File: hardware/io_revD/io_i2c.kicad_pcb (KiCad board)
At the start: 2 copper layers, 103.6 x 74.9 mm, 61 parts, among them J1 Target Interface, 2716 Pinout, J10 Conn_01x01, J11 Conn_01x01, J12 Conn_01x01, J13 Conn_01x01, J14 Conn_01x01, J15 Conn_01x01, J16 read region, J2 Jumper Block, J3 Jumper Block, J4 Target Interface, 2716 Pinout, J5 Conn_01x01, J6 Conn_01x01, J7 Conn_01x01, J8 Conn_01x01, J9 Conn_01x01, Q1 2N7000, U1 2716, U2 74HCT74, U3 74HCT125, U4 74HCT138, U6 MCP23018-E_SP, U7 74HCT138

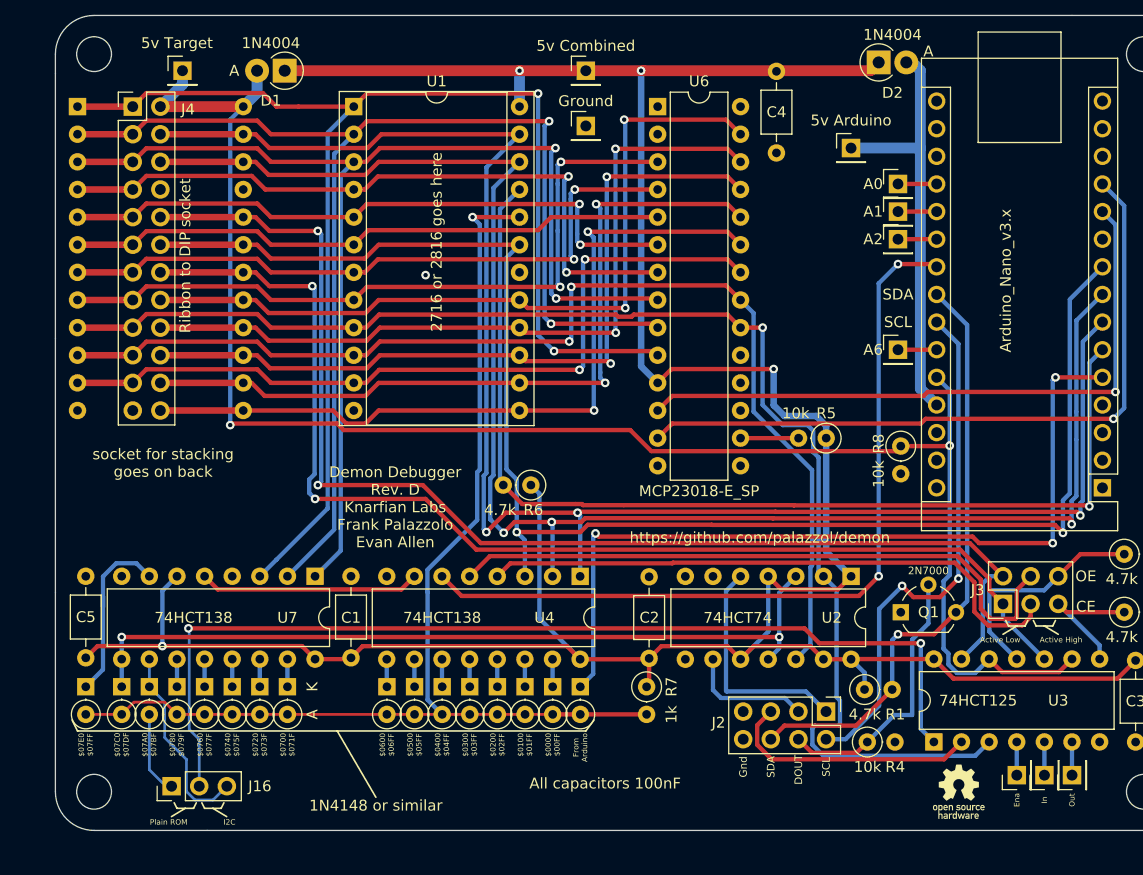
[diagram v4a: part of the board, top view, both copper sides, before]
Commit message: fixed silk, locations, and jumper
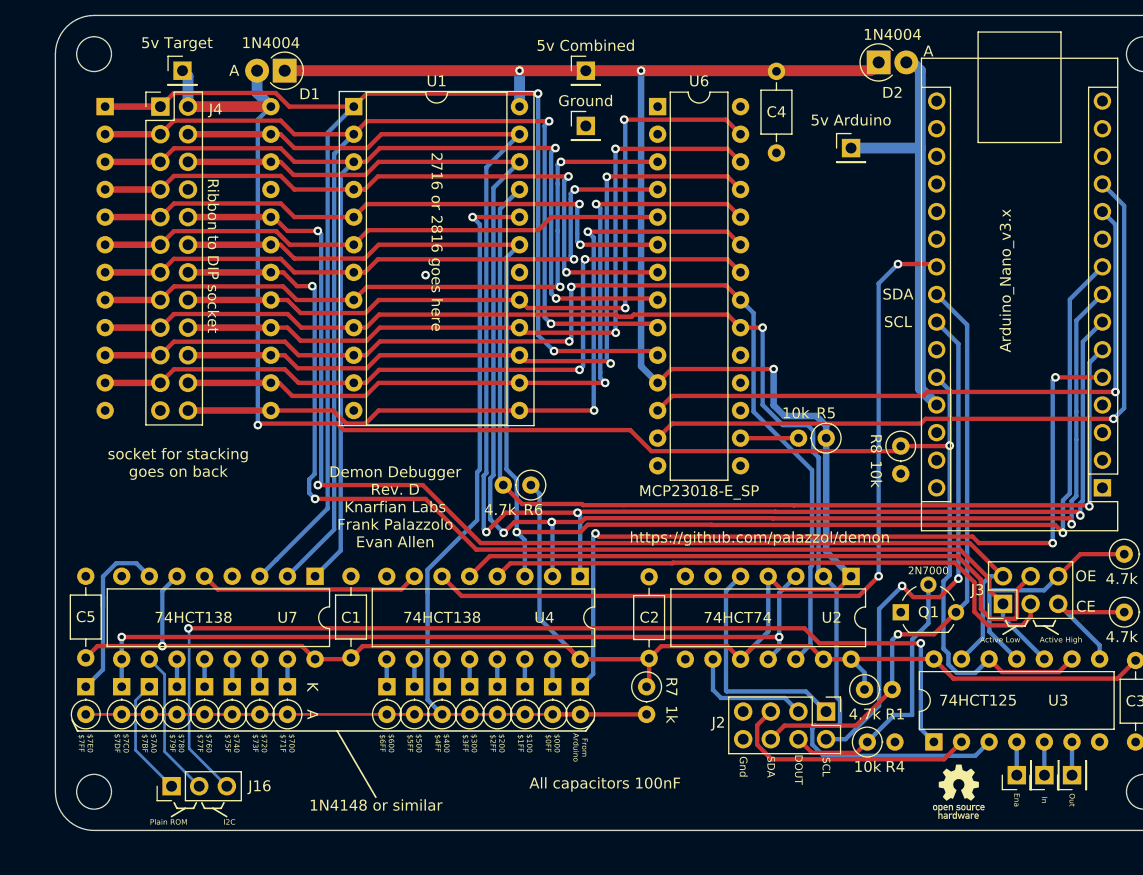
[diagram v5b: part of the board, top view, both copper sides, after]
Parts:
- removed J10, J11, J8, J9: Conn_01x01, Connector_PinHeader_2.54mm:PinHeader_1x01_P2.54mm_Vertical
- moved J1 2.54 mm to (89.2, 102.1)
- moved J4 2.54 mm to (94.2, 102.1)
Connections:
- A1 pad 19: Net-(A1-Pad19) -> unconnected-(A1-Pad19)
- A1 pad 20: Net-(A1-Pad20) -> unconnected-(A1-Pad20)
- A1 pad 21: Net-(A1-Pad21) -> unconnected-(A1-Pad21)
- A1 pad 25: Net-(A1-Pad25) -> unconnected-(A1-Pad25)
- D18 pad 1: Net-(U7-Pad10) -> Net-(D18-Pad1)
- D18 pad 2: Net-(D18-Pad2) -> Net-(D10-Pad2)
- J16 pad 1: Net-(D18-Pad2) -> Net-(D18-Pad1)
- J16 pad 2: Net-(U3-Pad1) -> Net-(U7-Pad10)
- J16 pad 3: Net-(U7-Pad10) -> Net-(J16-Pad3)
- U3 pad 1: Net-(U3-Pad1) -> Net-(J16-Pad3)
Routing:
- net Net-(J16-Pad3): track 0.00 -> 93.5 mm, vias 0 -> 2
- net Net-(U3-Pad1): track 92.4 -> 0.00 mm, vias 2 -> 0
- net Net-(D18-Pad1): track 0.00 -> 11.0 mm
- net Net-(D18-Pad2): track 7.76 -> 0.00 mm
- net Net-(U7-Pad10): track 18.1 -> 13.6 mm
- net Net-(A1-Pad25): track 3.56 -> 0.00 mm
- net Net-(A1-Pad21): track 3.56 -> 0.00 mm
- net Net-(A1-Pad20): track 3.56 -> 0.00 mm
- net Net-(A1-Pad19): track 3.56 -> 0.00 mm
- net +5VD: track 153.4 -> 150.2 mm
- net /Target OE: track 115.0 -> 112.4 mm
- net /D4: track 72.4 -> 69.9 mm
- net /A8: track 152.2 -> 149.7 mm
- net /A10: track 142.5 -> 140.0 mm
- net /Target CE: track 109.1 -> 106.5 mm
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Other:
- board text added: "$000 $0FF"
- board text added: "$100 $1FF"
- board text added: "$200 $2FF"
- board text added: "$300 $3FF"
- board text added: "$400 $4FF"
- board text added: "$500 $5FF"
- board text added: "$600 $6FF"
- board text added: "$700 $71F"
- board text added: "$720 $73F"
- board text added: "$740 $75F"
- board text added: "$760 $77F"
- board text added: "$780 $79F"
- board text added: "$7A0 $7BF"
- board text added: "$7C0 $7DF"
- board text added: "$7E0 $7FF"
- board text removed: "$0000 $00FF"
- board text removed: "$0100 $01FF"
- board text removed: "$0200 $02FF"
- board text removed: "$0300 $03FF"
- board text removed: "$0400 $04FF"
- board text removed: "$0500 $05FF"
- board text removed: "$0600 $06FF"
- board text removed: "$0700 $071F"
- board text removed: "$0720 $073F"
- board text removed: "$0740 $075F"
- board text removed: "$0760 $077F"
- board text removed: "$0780 $079F"
- board text removed: "$07A0 $07BF"
- board text removed: "$07C0 $07DF"
- board text removed: "$07E0 $07FF"
- board text removed: "A0"
- board text removed: "A1"
- board text removed: "A2"
- board text removed: "A6"

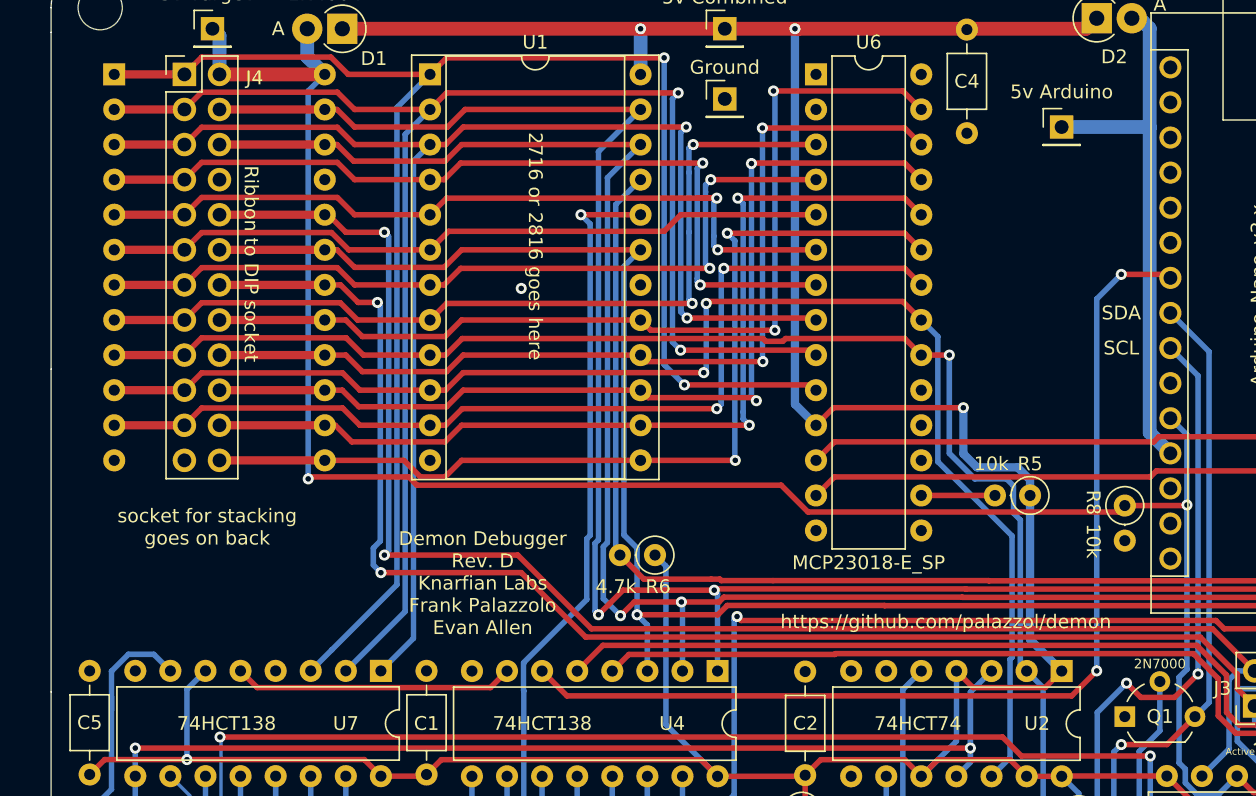
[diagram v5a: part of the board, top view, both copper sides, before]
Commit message: added layout change for extra CS mode
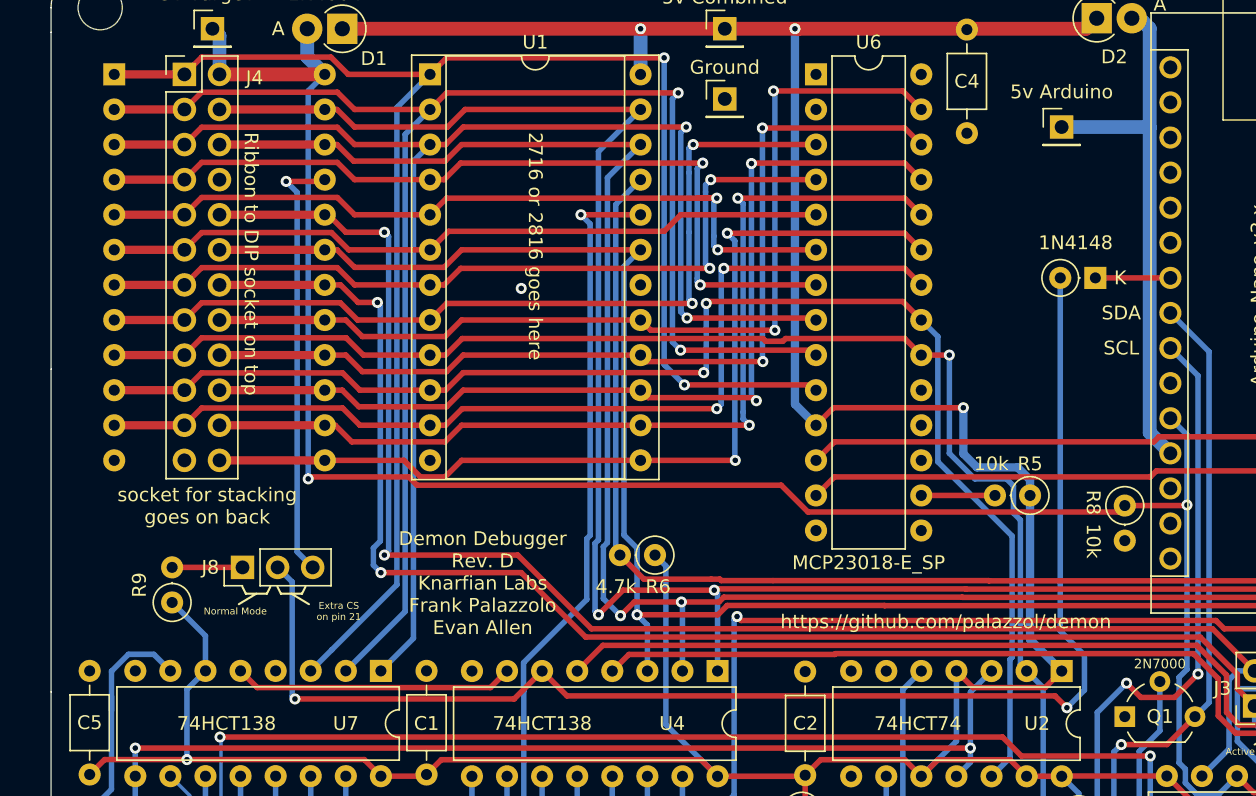
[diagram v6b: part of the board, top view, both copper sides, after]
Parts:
- added D19: 1N4148, Diode_THT:D_DO-35_SOD27_P2.54mm_Vertical_KathodeUp, F.Cu at (160.2, 116.8)
- added J8: extra CS, Connector_PinHeader_2.54mm:PinHeader_1x03_P2.54mm_Vertical, F.Cu at (98.4, 137.8)
- added R9: 4.7k, Resistor_THT:R_Axial_DIN0207_L6.3mm_D2.5mm_P2.54mm_Vertical, F.Cu at (93.3, 140.3)
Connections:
- A1 pad 22: /138 enable -> /arduino control CS
- J1 pad 21: unconnected-(J1-Pad21) -> /target VPP
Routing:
- net /target VPP: track 0.00 -> 31.6 mm, vias 0 -> 1
- net /138 enable: track 74.7 -> 100.2 mm
- net +5V: track 272.2 -> 278.1 mm
- net /arduino control CS: track 0.00 -> 5.43 mm
- net Net-(J8-Pad1): track 0.00 -> 5.09 mm
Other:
- board text added: "1N4148"
- board text added: "Extra CS on pin 21"
- board text added: "Normal Mode"
- board text added: "Ribbon to DIP socket on top"
- board text removed: "Ribbon to DIP socket"

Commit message: changed some ref des-es to make jumper numbering more sane
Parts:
- renumbered J8 to J1, J1 to J16, J16 to J5, J5 to J8
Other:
- board text added: "4.7k"
- board text added: "U6, C4, and fitting U1 with a 2816 enables onboard reprogramming of the flash chip"
- board text removed: "U6, C4, and U1 being a 2816 enables onboard reprogramming of the flash chip"
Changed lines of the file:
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@@
   (net 72 "Net-(D16-Pad1)")
   (net 73 "Net-(D17-Pad1)")
-  (net 74 "Net-(J5-Pad1)")
+  (net 74 "Net-(J1-Pad1)")
   (net 75 "/SCL2")
   (net 76 "/SDA2")
@@
   (net 83 "Net-(D10-Pad1)")
   (net 84 "/target VPP")
-  (net 85 "Net-(J16-Pad3)")
+  (net 85 "Net-(J5-Pad2)")
   (net 86 "unconnected-(A1-Pad19)")
   (net 87 "unconnected-(A1-Pad20)")
@@
   (net 89 "unconnected-(A1-Pad25)")
   (net 90 "Net-(J8-Pad1)")
-  (net 91 "Net-(J16-Pad2)")
+  (net 91 "Net-(J5-Pad3)")
   (footprint "Diode_THT:D_DO-35_SOD27_P2.54mm_Vertical_KathodeUp" (layer "F.Cu")
     (at 93.218 155.448 -90)
@@
     (property "Sheetname" "")
     (attr through_hole)
-    (fp_text reference "J1" (at 3.556 -2.33) (layer "B.SilkS")
+    (fp_text reference "J16" (at 3.556 -2.33) (layer "B.SilkS")
       (effects (font (size 1 1) (thickness 0.15)) (justify mirror))
     )
@@
       (net 72 "Net-(D16-Pad1)") (pinfunction "O6") (pintype "output"))
     (pad "10" thru_hole oval locked (at 7.62 15.24 270) (size 1.6 1.6) (drill 0.8) (layers *.Cu *.Mask)
-      (net 91 "Net-(J16-Pad2)") (pinfunction "O5") (pintype "output"))
+      (net 85 "Net-(J5-Pad2)") (pinfunction "O5") (pintype "output"))
     (pad "11" thru_hole oval locked (at 7.62 12.7 270) (size 1.6 1.6) (drill 0.8) (layers *.Cu *.Mask)
       (net 71 "Net-(D15-Pad1)") (pinfunction "O4") (pintype "output"))
@@
     (property "Sheetname" "")
     (attr through_hole)
-    (fp_text reference "J8" (at 0 -2.33 180) (layer "F.SilkS")
+    (fp_text reference "J1" (at 0 -2.33 180) (layer "F.SilkS")
       (effects (font (size 1 1) (thickness 0.15)))
     )
@@
     (fp_line (start -0.635 -1.27) (end 1.27 -1.27) (layer "F.Fab") (width 0.1))
     (pad "1" thru_hole rect locked (at 0 0 90) (size 1.7 1.7) (drill 1) (layers *.Cu *.Mask)
-      (net 90 "Net-(J8-Pad1)") (pinfunction "Pin_1") (pintype "passive"))
+      (net 74 "Net-(J1-Pad1)") (pinfunction "Pin_1") (pintype "passive"))
     (pad "2" thru_hole oval locked (at 0 2.54 90) (size 1.7 1.7) (drill 1) (layers *.Cu *.Mask)
       (net 37 "/138 enable") (pinfunction "Pin_2") (pintype "passive"))
@@
     (fp_line (start 1.635 -1.27) (end 6.985 -1.27) (layer "F.Fab") (width 0.1))
     (pad "1" thru_hole rect locked (at 0 0 90) (size 1.6 1.6) (drill 0.8) (layers *.Cu *.Mask)
-      (net 85 "Net-(J16-Pad3)") (pintype "input"))
+      (net 91 "Net-(J5-Pad3)") (pintype "input"))
     (pad "2" thru_hole oval locked (at 0 2.54 90) (size 1.6 1.6) (drill 0.8) (layers *.Cu *.Mask)
       (net 30 "Net-(J2-Pad5)") (pintype "input"))
@@
       (net 77 "Net-(J6-Pad1)") (pintype "input"))
     (pad "5" thru_hole oval locked (at 0 10.16 90) (size 1.6 1.6) (drill 0.8) (layers *.Cu *.Mask)
-      (net 74 "Net-(J5-Pad1)") (pintype "input"))
+      (net 90 "Net-(J8-Pad1)") (pintype "input"))
     (pad "6" thru_hole oval locked (at 0 12.7 90) (size 1.6 1.6) (drill 0.8) (layers *.Cu *.Mask)
       (net 78 "Net-(J7-Pad1)") (pintype "tri_state"))
@@
     (property "Sheetname" "")
     (attr through_hole)
-    (fp_text reference "J5" (at -2.286 0 90) (layer "F.SilkS") hide
+    (fp_text reference "J8" (at -2.286 0 90) (layer "F.SilkS") hide
       (effects (font (size 1 1) (thickness 0.15)))
     )
@@
     (fp_line (start 1.27 1.27) (end -1.27 1.27) (layer "F.Fab") (width 0.1))
     (pad "1" thru_hole rect locked (at 0 0 90) (size 1.7 1.7) (drill 1) (layers *.Cu *.Mask)
-      (net 74 "Net-(J5-Pad1)") (pinfunction "Pin_1") (pintype "passive"))
+      (net 90 "Net-(J8-Pad1)") (pinfunction "Pin_1") (pintype "passive"))
     (model "${KICAD6_3DMODEL_DIR}/Connector_PinHeader_2.54mm.3dshapes/PinHeader_1x01_P2.54mm_Vertical.wrl"
       (offset (xyz 0 0 0))
@@
     (property "Sheetname" "")
     (attr through_hole)
-    (fp_text reference "R9" (at 1.27 -2.37 90) (layer "F.SilkS")
+    (fp_text reference "R9" (at -0.635 -2.54 270 unlocked) (layer "F.SilkS")
       (effects (font (size 1 1) (thickness 0.15)))
     )
@@
       (net 3 "+5V") (pintype "passive"))
     (pad "2" thru_hole oval locked (at 2.54 0 90) (size 1.6 1.6) (drill 0.8) (layers *.Cu *.Mask)
-      (net 90 "Net-(J8-Pad1)") (pintype "passive"))
+      (net 74 "Net-(J1-Pad1)") (pintype "passive"))
     (model "${KICAD6_3DMODEL_DIR}/Resistor_THT.3dshapes/R_Axial_DIN0207_L6.3mm_D2.5mm_P2.54mm_Vertical.wrl"
       (offset (xyz 0 0 0))
@@
     (property "Sheetname" "")
     (attr through_hole)
-    (fp_text reference "J16" (at 0 8.113 180) (layer "F.SilkS")
+    (fp_text reference "J5" (at 0 8.113 180) (layer "F.SilkS")
       (effects (font (size 1 1) (thickness 0.15)))
     )
@@
       (net 61 "Net-(D18-Pad1)") (pinfunction "Pin_1") (pintype "passive"))
     (pad "2" thru_hole oval locked (at 0 2.54 90) (size 1.7 1.7) (drill 1) (layers *.Cu *.Mask)
-      (net 91 "Net-(J16-Pad2)") (pinfunction "Pin_2") (pintype "passive"))
+      (net 85 "Net-(J5-Pad2)") (pinfunction "Pin_2") (pintype "passive"))
     (pad "3" thru_hole oval locked (at 0 5.08 90) (size 1.7 1.7) (drill 1) (layers *.Cu *.Mask)
-      (net 85 "Net-(J16-Pad3)") (pinfunction "Pin_3") (pintype "passive"))
+      (net 91 "Net-(J5-Pad3)") (pinfunction "Pin_3") (pintype "passive"))
     (model "${KICAD6_3DMODEL_DIR}/Connector_PinHeader_2.54mm.3dshapes/PinHeader_1x03_P2.54mm_Vertical.wrl"
       (offset (xyz 0 0 0))
@@
     (effects (font (size 1 1) (thickness 0.15)) (justify mirror))
   )
-  (gr_text "U6, C4, and U1 being a 2816\nenables onboard reprogramming\nof the flash chip" (at 108.204 141.224) (layer "B.SilkS")
+  (gr_text "U6, C4, and fitting U1 with a 2816\nenables onboard reprogramming\nof the flash chip" (at 108.204 141.224) (layer "B.SilkS")
     (effects (font (size 1 1) (thickness 0.15)) (justify mirror))
   )
@@
     (effects (font (size 1 1) (thickness 0.15)))
   )
+  (gr_text "4.7k" (at 90.805 137.795 270) (layer "F.SilkS")
+    (effects (font (size 1 1) (thickness 0.15)))
+  )
   (gr_text "DOUT" (at 152.908 163.068 270) (layer "F.SilkS")
     (effects (font (size 0.7 0.7) (thickness 0.1)))
@@
   (segment (start 92.018489 144.088489) (end 90.181145 144.088489) (width 0.4) (layer "B.Cu") (net 73))
   (segment (start 87.376 155.448) (end 88.956511 153.867489) (width 0.4) (layer "B.Cu") (net 73))
-  (segment (start 175.509 160.518) (end 175.509 163.571) (width 0.4) (layer "B.Cu") (net 74))
-  (segment (start 175.509 163.571) (end 175.514 163.576) (width 0.4) (layer "B.Cu") (net 74))
+  (segment (start 93.345 137.795) (end 98.44 137.795) (width 0.4) (layer "F.Cu") (net 74))
   (segment (start 182.047511 128.340489) (end 164.775511 128.340489) (width 0.4) (layer "F.Cu") (net 75))
   (segment (start 164.408489 128.707511) (end 164.775511 128.340489) (width 0.4) (layer "F.Cu") (net 75))
@@
   (segment (start 102.394978 110.649978) (end 101.6 109.855) (width 0.4) (layer "B.Cu") (net 84))
   (segment (start 103.52 137.795) (end 102.394978 136.669978) (width 0.4) (layer "B.Cu") (net 84))
-  (segment (start 164.149489 151.449489) (end 154.826511 151.449489) (width 0.4) (layer "F.Cu") (net 85))
-  (segment (start 153.453511 150.076489) (end 96.811511 150.076489) (width 0.4) (layer "F.Cu") (net 85))
-  (segment (start 154.826511 151.449489) (end 153.453511 150.076489) (width 0.4) (layer "F.Cu") (net 85))
-  (via (at 164.149489 151.449489) (size 0.8) (drill 0.4) (layers "F.Cu" "B.Cu") (net 85))
-  (via (at 96.811511 150.076489) (size 0.8) (drill 0.4) (layers "F.Cu" "B.Cu") (net 85))
-  (segment (start 165.349 160.518) (end 164.149489 159.318489) (width 0.4) (layer "B.Cu") (net 85))
-  (segment (start 96.811511 150.076489) (end 96.882511 150.147489) (width 0.25) (layer "B.Cu") (net 85))
-  (segment (start 96.882511 150.147489) (end 96.882511 161.129511) (width 0.25) (layer "B.Cu") (net 85))
-  (segment (start 164.149489 159.318489) (end 164.149489 151.449489) (width 0.4) (layer "B.Cu") (net 85))
-  (segment (start 96.882511 161.129511) (end 100.345 164.592) (width 0.25) (layer "B.Cu") (net 85))
-  (segment (start 93.345 137.795) (end 98.44 137.795) (width 0.4) (layer "F.Cu") (net 90))
-  (segment (start 94.615 154.305) (end 94.615 161.402) (width 0.25) (layer "B.Cu") (net 91))
-  (segment (start 93.218 152.908) (end 94.615 154.305) (width 0.25) (layer "B.Cu") (net 91))
-  (segment (start 94.615 161.402) (end 97.805 164.592) (width 0.25) (layer "B.Cu") (net 91))
+  (segment (start 94.615 154.305) (end 94.615 161.402) (width 0.25) (layer "B.Cu") (net 85))
+  (segment (start 93.218 152.908) (end 94.615 154.305) (width 0.25) (layer "B.Cu") (net 85))
+  (segment (start 94.615 161.402) (end 97.805 164.592) (width 0.25) (layer "B.Cu") (net 85))
+  (segment (start 175.509 160.518) (end 175.509 163.571) (width 0.4) (layer "B.Cu") (net 90))
+  (segment (start 175.509 163.571) (end 175.514 163.576) (width 0.4) (layer "B.Cu") (net 90))
+  (segment (start 164.149489 151.449489) (end 154.826511 151.449489) (width 0.4) (layer "F.Cu") (net 91))
+  (segment (start 153.453511 150.076489) (end 96.811511 150.076489) (width 0.4) (layer "F.Cu") (net 91))
+  (segment (start 154.826511 151.449489) (end 153.453511 150.076489) (width 0.4) (layer "F.Cu") (net 91))
+  (via (at 164.149489 151.449489) (size 0.8) (drill 0.4) (layers "F.Cu" "B.Cu") (net 91))
+  (via (at 96.811511 150.076489) (size 0.8) (drill 0.4) (layers "F.Cu" "B.Cu") (net 91))
+  (segment (start 165.349 160.518) (end 164.149489 159.318489) (width 0.4) (layer "B.Cu") (net 91))
+  (segment (start 96.811511 150.076489) (end 96.882511 150.147489) (width 0.25) (layer "B.Cu") (net 91))
+  (segment (start 96.882511 150.147489) (end 96.882511 161.129511) (width 0.25) (layer "B.Cu") (net 91))
+  (segment (start 164.149489 159.318489) (end 164.149489 151.449489) (width 0.4) (layer "B.Cu") (net 91))
+  (segment (start 96.882511 161.129511) (end 100.345 164.592) (width 0.25) (layer "B.Cu") (net 91))
   (zone (net 1) (net_name "GND") (layers F&B.Cu) (hatch edge 0.508)
     (connect_pads (clearance 0.508))
